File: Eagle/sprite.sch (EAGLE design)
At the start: 39 parts

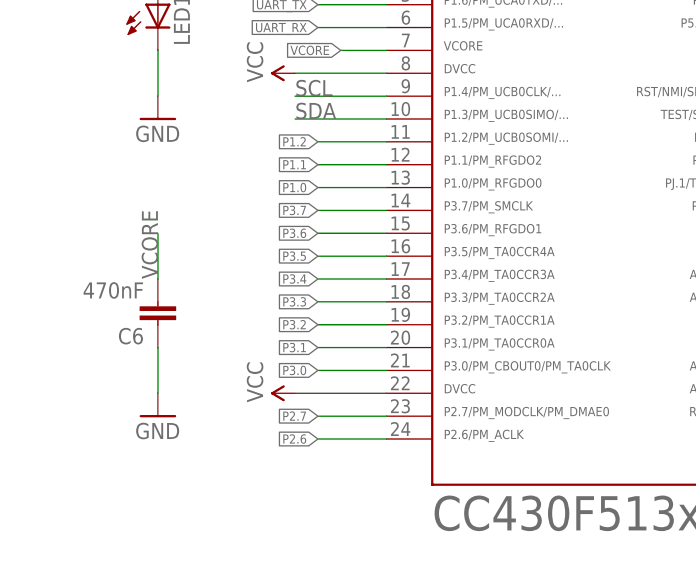
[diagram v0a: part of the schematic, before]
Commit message: Resized, still needs spacers
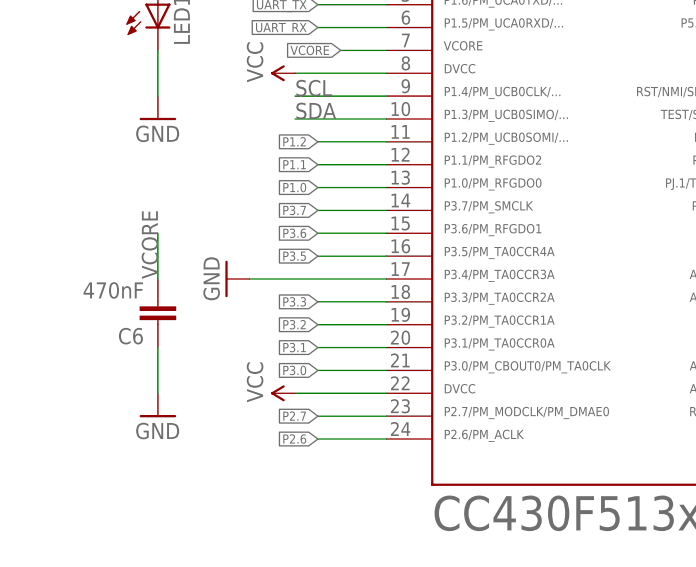
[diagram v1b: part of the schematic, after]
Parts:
- C1, C10, C11, C12, C2, C3, C4, C5, C6, C7, C8, C9: device SparkFun:CAP0805 -> SparkFun-Passives:CAP0402-CAP
- R1, R2, R3, R4, R5, R6, R7, R8: device SparkFun:RESISTOR0805-RES -> SparkFun-Passives:RESISTOR0402-RES
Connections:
- removed net P3.4: CC430.17
- net GND: now also CC430.17
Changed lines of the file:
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@@
 <part name="GND4" library="SparkFun" deviceset="GND" device=""/>
 <part name="GND5" library="SparkFun" deviceset="GND" device=""/>
-<part name="C1" library="SparkFun" deviceset="CAP" device="0805" value="0.1uF"/>
-<part name="C2" library="SparkFun" deviceset="CAP" device="0805" value="10nF"/>
-<part name="C3" library="SparkFun" deviceset="CAP" device="0805" value="0.1uF"/>
-<part name="C4" library="SparkFun" deviceset="CAP" device="0805" value="0.1uF"/>
-<part name="C5" library="SparkFun" deviceset="CAP" device="0805" value="10uF"/>
+<part name="C1" library="SparkFun-Passives" deviceset="CAP" device="0402-CAP" value="0.1uF"/>
+<part name="C2" library="SparkFun-Passives" deviceset="CAP" device="0402-CAP" value="10nF"/>
+<part name="C3" library="SparkFun-Passives" deviceset="CAP" device="0402-CAP" value="0.1uF"/>
+<part name="C4" library="SparkFun-Passives" deviceset="CAP" device="0402-CAP" value="0.1uF"/>
+<part name="C5" library="SparkFun-Passives" deviceset="CAP" device="0402-CAP" value="10uF"/>
 <part name="P+1" library="SparkFun" deviceset="VCC" device=""/>
-<part name="R1" library="SparkFun" deviceset="RESISTOR" device="0805-RES" value="10K"/>
+<part name="R1" library="SparkFun-Passives" deviceset="RESISTOR" device="0402-RES" value="10K"/>
 <part name="P+2" library="SparkFun" deviceset="VCC" device=""/>
-<part name="R2" library="SparkFun" deviceset="RESISTOR" device="0805-RES" value="10K"/>
-<part name="R3" library="SparkFun" deviceset="RESISTOR" device="0805-RES" value="10K"/>
+<part name="R2" library="SparkFun-Passives" deviceset="RESISTOR" device="0402-RES" value="10K"/>
+<part name="R3" library="SparkFun-Passives" deviceset="RESISTOR" device="0402-RES" value="10K"/>
 <part name="P+3" library="SparkFun" deviceset="VCC" device=""/>
 <part name="P+4" library="SparkFun" deviceset="VCC" device=""/>
 <part name="CC430" library="TI_MSP430_v16" deviceset="CC430F513X---RGZ48" device=""/>
-<part name="C6" library="SparkFun" deviceset="CAP" device="0805" value="470nF"/>
+<part name="C6" library="SparkFun-Passives" deviceset="CAP" device="0402-CAP" value="470nF"/>
 <part name="GND6" library="SparkFun" deviceset="GND" device=""/>
 <part name="P+5" library="SparkFun" deviceset="VCC" device=""/>
@@
 <part name="GND9" library="SparkFun" deviceset="GND" device=""/>
 <part name="GND10" library="SparkFun" deviceset="GND" device=""/>
-<part name="R4" library="SparkFun" deviceset="RESISTOR" device="0805-RES" value="10K"/>
-<part name="R5" library="SparkFun" deviceset="RESISTOR" device="0805-RES" value="10K"/>
+<part name="R4" library="SparkFun-Passives" deviceset="RESISTOR" device="0402-RES" value="10K"/>
+<part name="R5" library="SparkFun-Passives" deviceset="RESISTOR" device="0402-RES" value="10K"/>
 <part name="GND11" library="SparkFun" deviceset="GND" device=""/>
 <part name="P+9" library="SparkFun" deviceset="VCC" device=""/>
-<part name="R6" library="SparkFun" deviceset="RESISTOR" device="0805-RES" value="56K"/>
+<part name="R6" library="SparkFun-Passives" deviceset="RESISTOR" device="0402-RES" value="56K"/>
 <part name="GND12" library="SparkFun" deviceset="GND" device=""/>
 <part name="P+10" library="SparkFun" deviceset="VCC" device=""/>
 <part name="SPRITE" library="frames" deviceset="A3L-LOC" device=""/>
-<part name="C8" library="SparkFun" deviceset="CAP" device="0805" value="10nF"/>
-<part name="C9" library="SparkFun" deviceset="CAP" device="0805" value="0.1uF"/>
+<part name="C8" library="SparkFun-Passives" deviceset="CAP" device="0402-CAP" value="10nF"/>
+<part name="C9" library="SparkFun-Passives" deviceset="CAP" device="0402-CAP" value="0.1uF"/>
 <part name="GND14" library="SparkFun" deviceset="GND" device=""/>
 <part name="GND15" library="SparkFun" deviceset="GND" device=""/>
 <part name="L1" library="SparkFun" deviceset="INDUCTOR" device="0402" value="12nH"/>
 <part name="P+12" library="SparkFun" deviceset="VCC" device=""/>
-<part name="C10" library="SparkFun" deviceset="CAP" device="0805" value="470nF"/>
+<part name="C10" library="SparkFun-Passives" deviceset="CAP" device="0402-CAP" value="470nF"/>
 <part name="GND16" library="SparkFun" deviceset="GND" device=""/>
 <part name="GND21" library="SparkFun" deviceset="GND" device=""/>
 <part name="P+15" library="SparkFun" deviceset="VCC" device=""/>
-<part name="C7" library="SparkFun" deviceset="CAP" device="0805" value="10uF"/>
+<part name="C7" library="SparkFun-Passives" deviceset="CAP" device="0402-CAP" value="10uF"/>
 <part name="GND22" library="SparkFun" deviceset="GND" device=""/>
 <part name="32KHZ" library="SpriteCrystal" deviceset="SPRITECRYSTAL" device="SPRITECRYSTAL"/>
 <part name="JP3" library="SparkFun" deviceset="M02" device="PTH"/>
-<part name="R7" library="SparkFun" deviceset="RESISTOR" device="0805-RES" value="56K"/>
+<part name="R7" library="SparkFun-Passives" deviceset="RESISTOR" device="0402-RES" value="56K"/>
 <part name="JP1" library="SparkFun" deviceset="M02" device="PTH"/>
 <part name="TRISOL2" library="TriSolX_QzQube" deviceset="TRISOLX-WING" device=""/>
@@
 <part name="P+14" library="SparkFun" deviceset="VCC" device=""/>
 <part name="TXCO" library="SpriteTCXO" deviceset="TCXO_7Z" device=""/>
-<part name="C11" library="SparkFun" deviceset="CAP" device="0805" value="10nF"/>
+<part name="C11" library="SparkFun-Passives" deviceset="CAP" device="0402-CAP" value="10nF"/>
 <part name="GND19" library="SparkFun" deviceset="GND" device=""/>
 <part name="P+16" library="SparkFun" deviceset="VCC" device=""/>
 <part name="P+22" library="SparkFun" deviceset="VCC" device=""/>
-<part name="R8" library="SparkFun" deviceset="RESISTOR" device="0805-RES" value="1K"/>
-<part name="C12" library="SparkFun" deviceset="CAP" device="0805" value="10uF"/>
+<part name="R8" library="SparkFun-Passives" deviceset="RESISTOR" device="0402-RES" value="1K"/>
+<part name="C12" library="SparkFun-Passives" deviceset="CAP" device="0402-CAP" value="10uF"/>
 <part name="GND20" library="SparkFun" deviceset="GND" device=""/>
 <part name="JP2" library="SparkFun" deviceset="M02" device="PTH"/>
 <part name="P+11" library="SparkFun" deviceset="VCC" device=""/>
 <part name="GND13" library="SparkFun" deviceset="GND" device=""/>
+<part name="GND23" library="SparkFun" deviceset="GND" device=""/>
 </parts>
 <sheets>
@@
 <instance part="P+11" gate="1" x="190.5" y="93.98" rot="R90"/>
 <instance part="GND13" gate="1" x="187.96" y="86.36" rot="R270"/>
+<instance part="GND23" gate="1" x="27.94" y="91.44" rot="R270"/>
 </instances>
 <busses>
@@
 <pinref part="JP2" gate="G$1" pin="2"/>
 <wire x1="193.04" y1="88.9" x2="198.12" y2="88.9" width="0.1524" layer="91"/>
+</segment>
+<segment>
+<pinref part="GND23" gate="1" pin="GND"/>
+<pinref part="CC430" gate="G$1" pin="17"/>
+<wire x1="30.48" y1="91.44" x2="45.72" y2="91.44" width="0.1524" layer="91"/>
 </segment>
 </net>
@@
 </segment>
 </net>
-<net name="P3.4" class="0">
-<segment>
-<pinref part="CC430" gate="G$1" pin="17"/>
-<wire x1="45.72" y1="91.44" x2="38.1" y2="91.44" width="0.1524" layer="91"/>
-<label x="38.1" y="91.44" size="1.016" layer="95" rot="R180" xref="yes"/>
-</segment>
-</net>
